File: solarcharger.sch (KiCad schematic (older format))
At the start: 8 parts, among them K1 RELAY_SPDT_DELAY_10SEC, P1 CONN_01X04, P2 CONN_01X04, U1 SOLAR_PANEL, U2 SOLAR_CHARGER

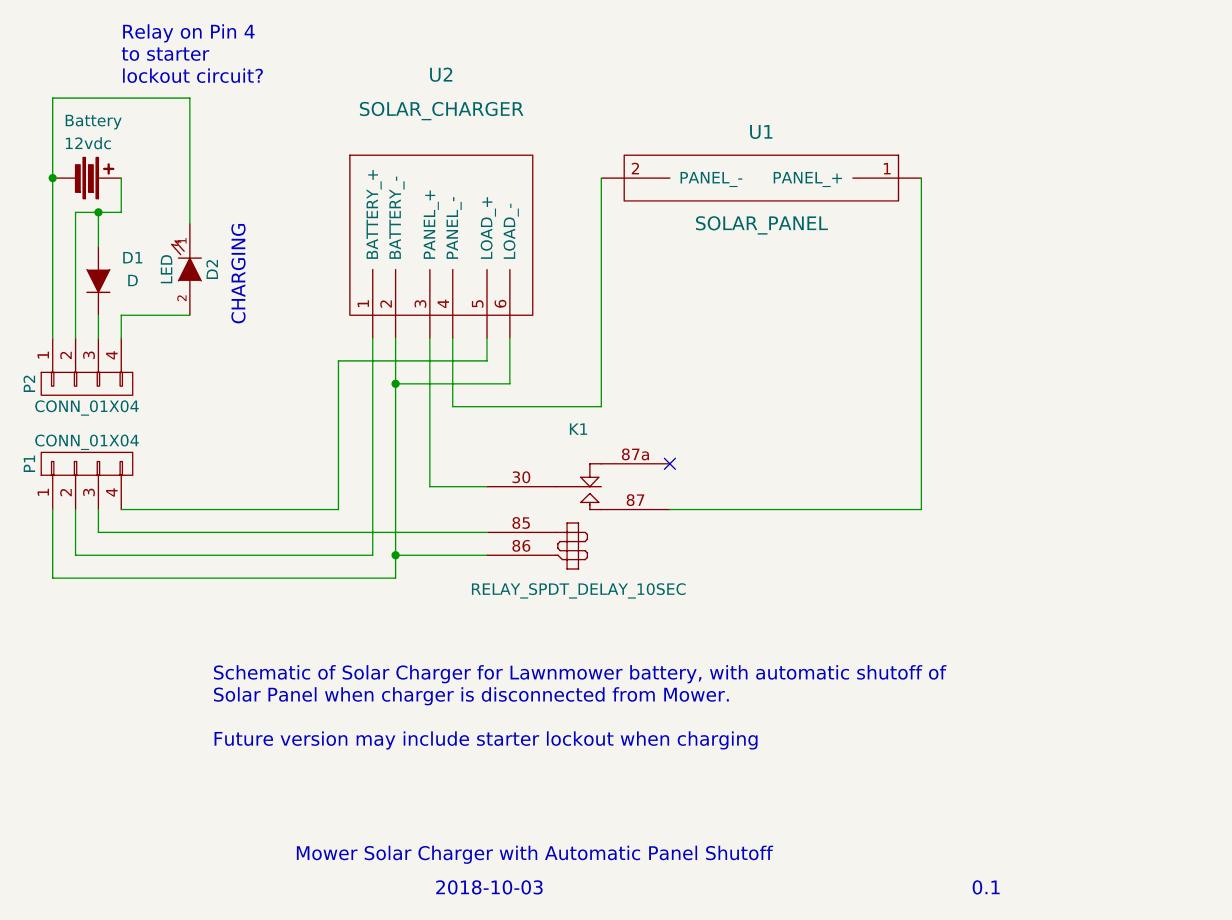
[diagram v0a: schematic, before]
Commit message: Corrected critical flaw that prevented panel disconnection
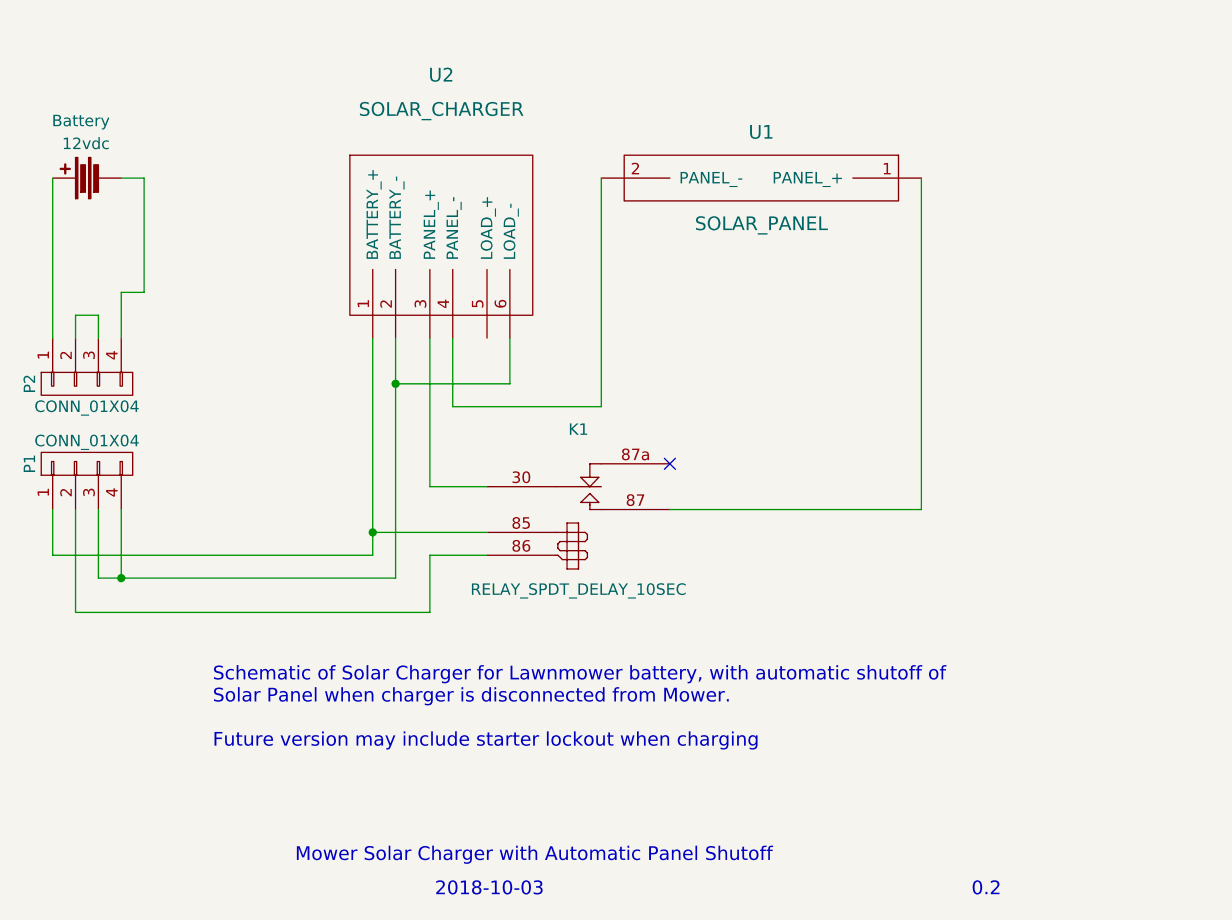
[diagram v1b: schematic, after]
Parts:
- removed D1: D, symbol D
- removed D2: LED, symbol LED
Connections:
- net at 12vdc.1: now also P2.1 (P1); no longer P2.2 (P2)
- net at 12vdc.2: now also P2.4 (P4); no longer P2.1 (P1)
- net at U2.1 (BATTERY_+): now also K1.85, P1.1 (P1); no longer P1.2 (P2)
- net at U2.2 (BATTERY_-), U2.6 (LOAD_-): now also P1.3 (P3), P1.4 (P4); no longer K1.86, P1.1 (P1)
- net at U2.5 (LOAD_+): no longer P1.4 (P4)
- net at P2.3 (P3): now also P2.2 (P2)
- new net: K1.86, P1.2 (P2)
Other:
- note added: "0.2"
- note removed: "0.1"
- note removed: "CHARGING"
- note removed: "Relay on Pin 4\nto starter\nlockout circuit?"
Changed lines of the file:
@@
 F 3 "" V 1000 1390 50  0000 C CNN
 	1    1000 1350
-	0    1    -1   0
+	0    -1   -1   0
 $EndComp
 $Comp
@@
 	0    -1   1    0
 $EndComp
-$Comp
-L D D1
-U 1 1 5BB5B914
-P 1050 1800
-F 0 "D1" V 1150 1650 50  0000 C CNN
-F 1 "D" V 1050 1650 50  0000 C CNN
-F 2 "" H 1050 1800 50  0000 C CNN
-F 3 "" H 1050 1800 50  0000 C CNN
-	1    1050 1800
-	0    -1   -1   0
-$EndComp
 NoConn ~ 3550 2600
-Wire Wire Line
-	3250 1350 3250 2350
-Wire Wire Line
-	3250 2350 2600 2350
-Wire Wire Line
-	2600 2350 2600 2050
-Wire Wire Line
-	4650 2800 3550 2800
-Wire Wire Line
-	2750 2700 2500 2700
-Wire Wire Line
-	850  1000 850  2050
-Wire Wire Line
-	1150 1500 1150 1350
-Wire Wire Line
-	950  1500 1150 1500
-Wire Wire Line
-	950  1500 950  2050
-Wire Wire Line
-	1050 1650 1050 1500
-Connection ~ 1050 1500
-Wire Wire Line
-	1050 1950 1050 2050
-Wire Wire Line
-	950  2800 950  3000
-Wire Wire Line
-	950  3000 2250 3000
-Wire Wire Line
-	2250 3000 2250 2050
-Wire Wire Line
-	850  2800 850  3100
-Wire Wire Line
-	850  3100 2350 3100
-Wire Wire Line
-	2350 3100 2350 2050
-Wire Wire Line
-	2750 3000 2350 3000
-Connection ~ 2350 3000
-Wire Wire Line
-	2750 2900 1050 2900
-Wire Wire Line
-	1050 2900 1050 2800
-Wire Wire Line
-	2500 2700 2500 2050
-Wire Wire Line
-	4650 2800 4650 1350
-Wire Wire Line
-	2850 2050 2850 2250
-Wire Wire Line
-	2850 2250 2350 2250
-Connection ~ 2350 2250
-Wire Wire Line
-	2750 2050 2750 2150
-Wire Wire Line
-	2750 2150 2100 2150
-Wire Wire Line
-	2100 2150 2100 2800
-Wire Wire Line
-	2100 2800 1150 2800
-$Comp
-L LED D2
-U 1 1 5BB5C4DB
-P 1450 1750
-F 0 "D2" H 1450 1850 50  0000 C CNN
-F 1 "LED" H 1450 1650 50  0000 C CNN
-F 2 "" H 1450 1750 50  0000 C CNN
-F 3 "" H 1450 1750 50  0000 C CNN
-	1    1450 1750
-	0    1    1    0
-$EndComp
-Wire Wire Line
-	1150 2050 1150 1950
-Wire Wire Line
-	1150 1950 1450 1950
-Wire Wire Line
-	1450 1550 1450 1000
-Wire Wire Line
-	1450 1000 850  1000
-Connection ~ 850  1350
-Text Notes 1700 2000 1    60   ~ 0
-CHARGING
-Text Notes 1150 950  0    60   ~ 0
-Relay on Pin 4\nto starter\nlockout circuit?
 Text Notes 4000 4350 2    60   ~ 0
 Mower Solar Charger with Automatic Panel Shutoff
@@
 2018-10-03
 Text Notes 5000 4500 2    60   ~ 0
-0.1
+0.2
 Text Notes 1550 3850 0    60   ~ 0
 Schematic of Solar Charger for Lawnmower battery, with automatic shutoff of\nSolar Panel when charger is disconnected from Mower.\n\nFuture version may include starter lockout when charging
+Connection ~ 2250 2900
+Wire Wire Line
+	850  3000 850  2800
+Wire Wire Line
+	2250 3000 850  3000
+Wire Wire Line
+	1250 1850 1250 1350
+Wire Wire Line
+	850  2050 850  1350
+Connection ~ 2350 2250
+Wire Wire Line
+	2850 2250 2350 2250
+Wire Wire Line
+	2850 2050 2850 2250
+Wire Wire Line
+	4650 2800 4650 1350
+Wire Wire Line
+	2500 2700 2500 2050
+Wire Wire Line
+	2350 3100 2350 2050
+Wire Wire Line
+	2250 3000 2250 2050
+Wire Wire Line
+	2750 2700 2500 2700
+Wire Wire Line
+	4650 2800 3550 2800
+Wire Wire Line
+	2600 2350 2600 2050
+Wire Wire Line
+	3250 2350 2600 2350
+Wire Wire Line
+	3250 1350 3250 2350
+Wire Wire Line
+	2750 2900 2250 2900
+Wire Wire Line
+	1250 1350 1150 1350
+Wire Wire Line
+	1150 2050 1150 1850
+Wire Wire Line
+	1150 1850 1250 1850
+Wire Wire Line
+	1050 3100 2350 3100
+Wire Wire Line
+	1150 3100 1150 2800
+Wire Wire Line
+	1050 2050 1050 1950
+Wire Wire Line
+	1050 1950 950  1950
+Wire Wire Line
+	950  1950 950  2050
+Wire Wire Line
+	1050 3100 1050 2800
+Connection ~ 1150 3100
+Wire Wire Line
+	950  2800 950  3250
+Wire Wire Line
+	950  3250 2500 3250
+Wire Wire Line
+	2500 3250 2500 3000
+Wire Wire Line
+	2500 3000 2750 3000
 $EndSCHEMATC
